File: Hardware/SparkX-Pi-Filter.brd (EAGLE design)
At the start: 25.4 x 25.4 mm, 27 parts

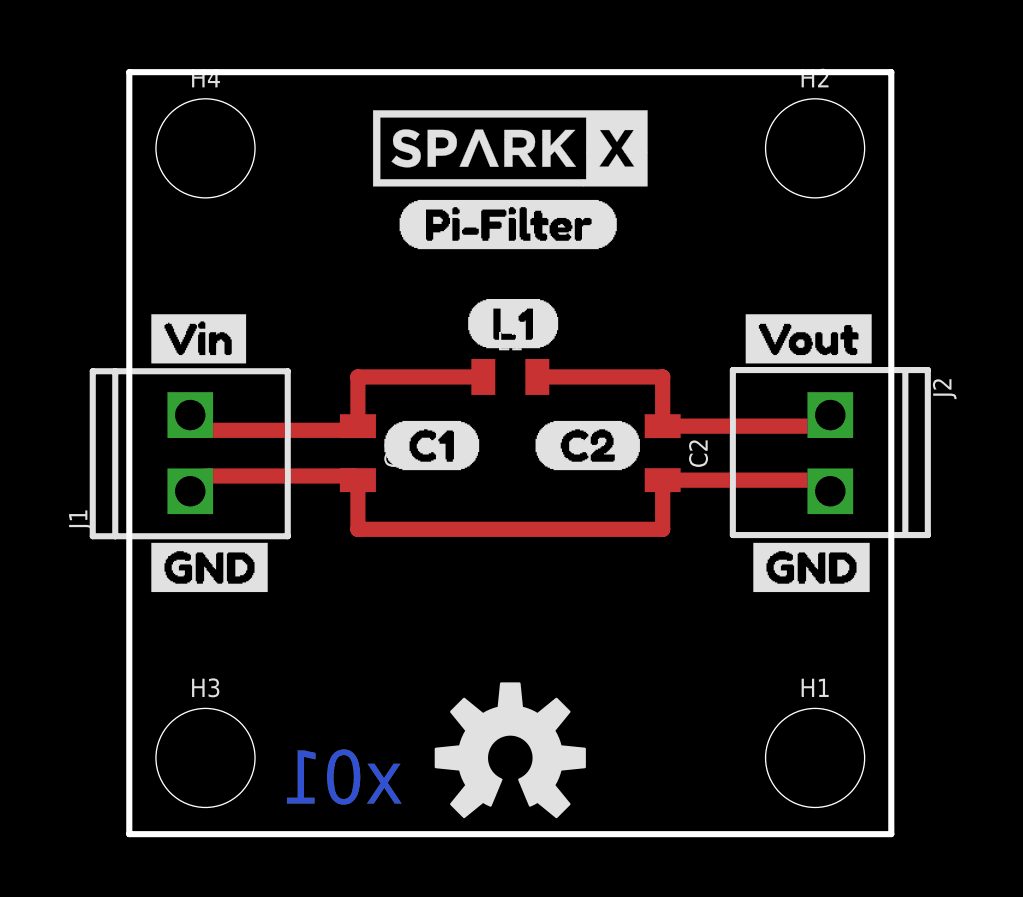
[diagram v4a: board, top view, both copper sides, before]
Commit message: Mitre square traces. Add production gerbers.
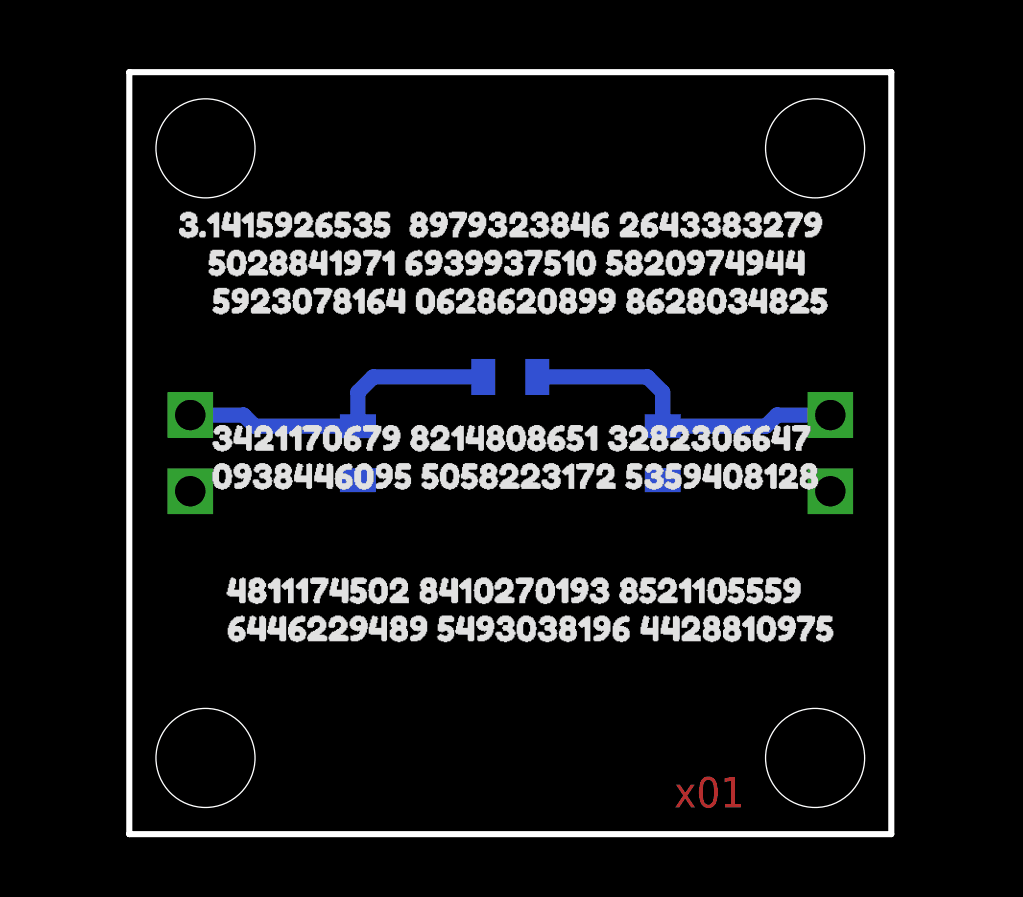
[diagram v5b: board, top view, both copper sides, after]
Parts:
- moved FRAME1 43.2 mm to (34.3, -17.8), flipped to the bottom
- moved U$3 24.9 mm to (25.1, 8.89), flipped to the bottom
- moved U$5 24.9 mm to (25.1, 16.5), flipped to the bottom
- moved U$6 23.6 mm to (0.89, 20.3), flipped to the top
- moved U$7 21.6 mm to (1.91, 19.1), flipped to the top
- moved J1 21.3 mm to (23.4, 11.4), flipped to the bottom
- moved J2 21.3 mm to (2.03, 14.0), flipped to the bottom
- moved U$10 21.3 mm to (2.03, 11.9), flipped to the top
- moved U$8 21.3 mm to (2.03, 17.8), flipped to the top
- moved U$9 21.3 mm to (2.03, 13.2), flipped to the top
- moved H1 20.3 mm to (2.54, 2.54), flipped to the bottom
- moved H2 20.3 mm to (2.54, 22.9), flipped to the bottom
- moved H3 20.3 mm to (22.9, 2.54), flipped to the bottom
- moved H4 20.3 mm to (22.9, 22.9), flipped to the bottom
- moved U$11 20.3 mm to (2.54, 8.13), flipped to the top
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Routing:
- net GND: track 25.0 -> 1.44 mm
- added copper zone on layer 16, net GND
- removed copper zone on layer 1, net GND
